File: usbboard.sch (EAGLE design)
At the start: 2 parts

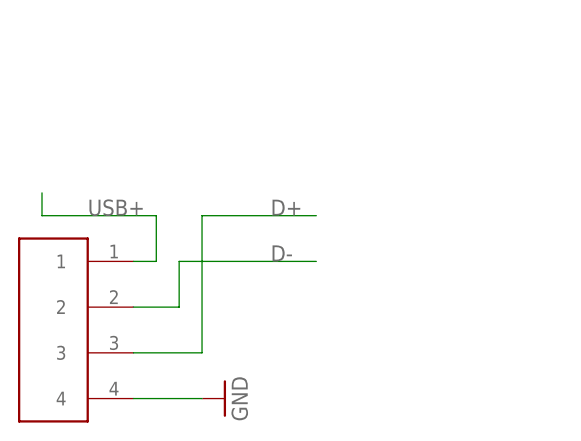
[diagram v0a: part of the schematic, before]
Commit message: fixed intial board errors, including short, flipped usb, and missing trace
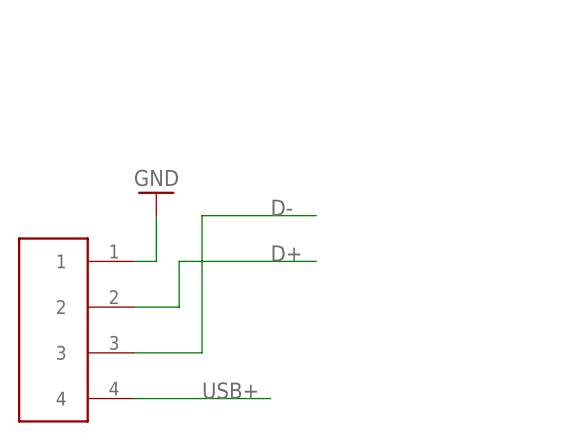
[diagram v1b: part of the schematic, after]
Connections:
- net D+: now also U$3.2; no longer U$3.3
- net D-: now also U$3.3; no longer U$3.2
- net GND: now also U$3.1; no longer U$3.4
- net USB+: now also U$3.4; no longer U$3.1
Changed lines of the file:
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@@
 <instance part="MICRO-USB" gate="G$1" x="114.3" y="177.8"/>
 <instance part="U$3" gate="G$1" x="17.78" y="119.38"/>
-<instance part="GND7" gate="1" x="33.02" y="111.76" rot="R90"/>
+<instance part="GND7" gate="1" x="25.4" y="134.62" rot="R180"/>
 <instance part="GND14" gate="1" x="121.92" y="167.64"/>
 </instances>
@@
 </segment>
 <segment>
-<pinref part="U$3" gate="G$1" pin="4"/>
-<wire x1="22.86" y1="111.76" x2="30.48" y2="111.76" width="0.1524" layer="91"/>
-<pinref part="GND7" gate="1" pin="GND"/>
-</segment>
-<segment>
 <pinref part="MICRO-USB" gate="G$1" pin="GND"/>
 <wire x1="119.38" y1="172.72" x2="121.92" y2="172.72" width="0.1524" layer="91"/>
@@
 <wire x1="121.92" y1="170.18" x2="121.92" y2="172.72" width="0.1524" layer="91"/>
 </segment>
+<segment>
+<pinref part="U$3" gate="G$1" pin="1"/>
+<pinref part="GND7" gate="1" pin="GND"/>
+<wire x1="22.86" y1="127" x2="25.4" y2="127" width="0.1524" layer="91"/>
+<wire x1="25.4" y1="127" x2="25.4" y2="132.08" width="0.1524" layer="91"/>
+</segment>
 </net>
 <net name="D+" class="0">
+<segment>
+<pinref part="MICRO-USB" gate="G$1" pin="D+"/>
+<wire x1="119.38" y1="177.8" x2="124.46" y2="177.8" width="0.1524" layer="91"/>
+<label x="121.92" y="177.8" size="1.778" layer="95"/>
+</segment>
+<segment>
+<label x="38.1" y="127" size="1.778" layer="95"/>
+<wire x1="43.18" y1="127" x2="27.94" y2="127" width="0.1524" layer="91"/>
+<wire x1="27.94" y1="127" x2="27.94" y2="121.92" width="0.1524" layer="91"/>
+<pinref part="U$3" gate="G$1" pin="2"/>
+<wire x1="27.94" y1="121.92" x2="22.86" y2="121.92" width="0.1524" layer="91"/>
+</segment>
+</net>
+<net name="D-" class="0">
+<segment>
+<pinref part="MICRO-USB" gate="G$1" pin="D-"/>
+<wire x1="119.38" y1="180.34" x2="124.46" y2="180.34" width="0.1524" layer="91"/>
+<label x="121.92" y="180.34" size="1.778" layer="95"/>
+</segment>
 <segment>
 <label x="38.1" y="132.08" size="1.778" layer="95"/>
@@
 <wire x1="30.48" y1="116.84" x2="22.86" y2="116.84" width="0.1524" layer="91"/>
 </segment>
-<segment>
-<pinref part="MICRO-USB" gate="G$1" pin="D+"/>
-<wire x1="119.38" y1="177.8" x2="124.46" y2="177.8" width="0.1524" layer="91"/>
-<label x="121.92" y="177.8" size="1.778" layer="95"/>
-</segment>
-</net>
-<net name="D-" class="0">
-<segment>
-<label x="38.1" y="127" size="1.778" layer="95"/>
-<wire x1="43.18" y1="127" x2="27.94" y2="127" width="0.1524" layer="91"/>
-<wire x1="27.94" y1="127" x2="27.94" y2="121.92" width="0.1524" layer="91"/>
-<pinref part="U$3" gate="G$1" pin="2"/>
-<wire x1="27.94" y1="121.92" x2="22.86" y2="121.92" width="0.1524" layer="91"/>
-</segment>
-<segment>
-<pinref part="MICRO-USB" gate="G$1" pin="D-"/>
-<wire x1="119.38" y1="180.34" x2="124.46" y2="180.34" width="0.1524" layer="91"/>
-<label x="121.92" y="180.34" size="1.778" layer="95"/>
-</segment>
 </net>
 <net name="USB+" class="0">
-<segment>
-<wire x1="12.7" y1="134.62" x2="12.7" y2="132.08" width="0.1524" layer="91"/>
-<wire x1="12.7" y1="132.08" x2="25.4" y2="132.08" width="0.1524" layer="91"/>
-<wire x1="25.4" y1="132.08" x2="25.4" y2="127" width="0.1524" layer="91"/>
-<pinref part="U$3" gate="G$1" pin="1"/>
-<wire x1="25.4" y1="127" x2="22.86" y2="127" width="0.1524" layer="91"/>
-<label x="17.78" y="132.08" size="1.778" layer="95"/>
-</segment>
 <segment>
 <pinref part="MICRO-USB" gate="G$1" pin="V+"/>
@@
 <label x="121.92" y="182.88" size="1.778" layer="95"/>
 </segment>
+<segment>
+<pinref part="U$3" gate="G$1" pin="4"/>
+<wire x1="22.86" y1="111.76" x2="38.1" y2="111.76" width="0.1524" layer="91"/>
+<label x="30.48" y="111.76" size="1.778" layer="95"/>
+</segment>
 </net>
